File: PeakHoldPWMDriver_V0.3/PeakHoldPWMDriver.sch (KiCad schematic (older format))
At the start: 121 parts, among them J1 RND 205-00203, J2 RND 205-00205, Q1 2N7002, Q10 2N7002, Q11 2N7002, Q12 2N7002, Q13 TSM2309, Q14 IRLL 024N, Q15 TSM2309, Q16 IRLL 024N, Q17 TSM2309, Q18 TSM2309, Q19 TSM2309, Q2 2N7002, Q20 TSM2309, Q3 2N7002, Q4 2N7002, Q5 TSM2309, Q6 TSM2309, Q7 IRLL 024N, Q8 IRLL 024N, Q9 2N7002, U1 74LS32, U2 LM2901, U3 74LS74, U4 LTC6992, U5 74LS74, U6 LM340, U7 74LS08, U8 74LS08, U9 LM2904

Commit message: Some leftover updates
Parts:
- gave numbers to parts that had none: 1
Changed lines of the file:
@@
 	650  6550 700  6550
 $Comp
-L Amplifier_Operational:LM2904 U?
+L Amplifier_Operational:LM2904 U9
 U 2 1 5F7AED14
 P 1600 5700
-F 0 "U?" H 1600 6067 50  0000 C CNN
+F 0 "U9" H 1600 6067 50  0000 C CNN
 F 1 "LM2904" H 1600 5976 50  0000 C CNN
 F 2 "Package_SO:SO-8_3.9x4.9mm_P1.27mm" H 1600 5700 50  0001 C CNN

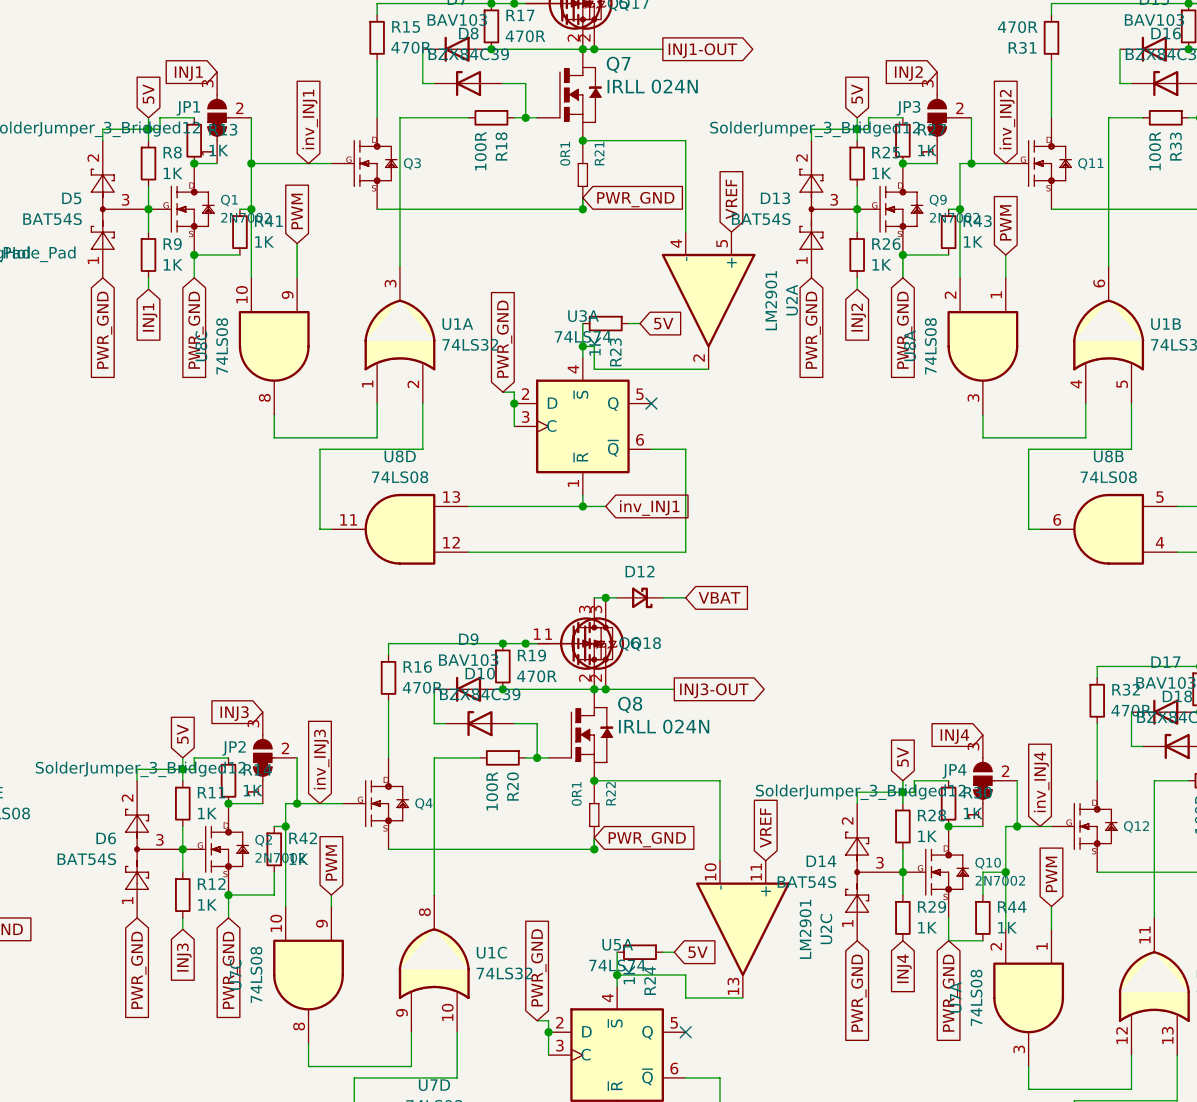
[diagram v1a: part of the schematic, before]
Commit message: updates values on 0.3 added 0.3.1
Updated resistor values for V0.3
Added V0.3.1 with new battery voltage compensation
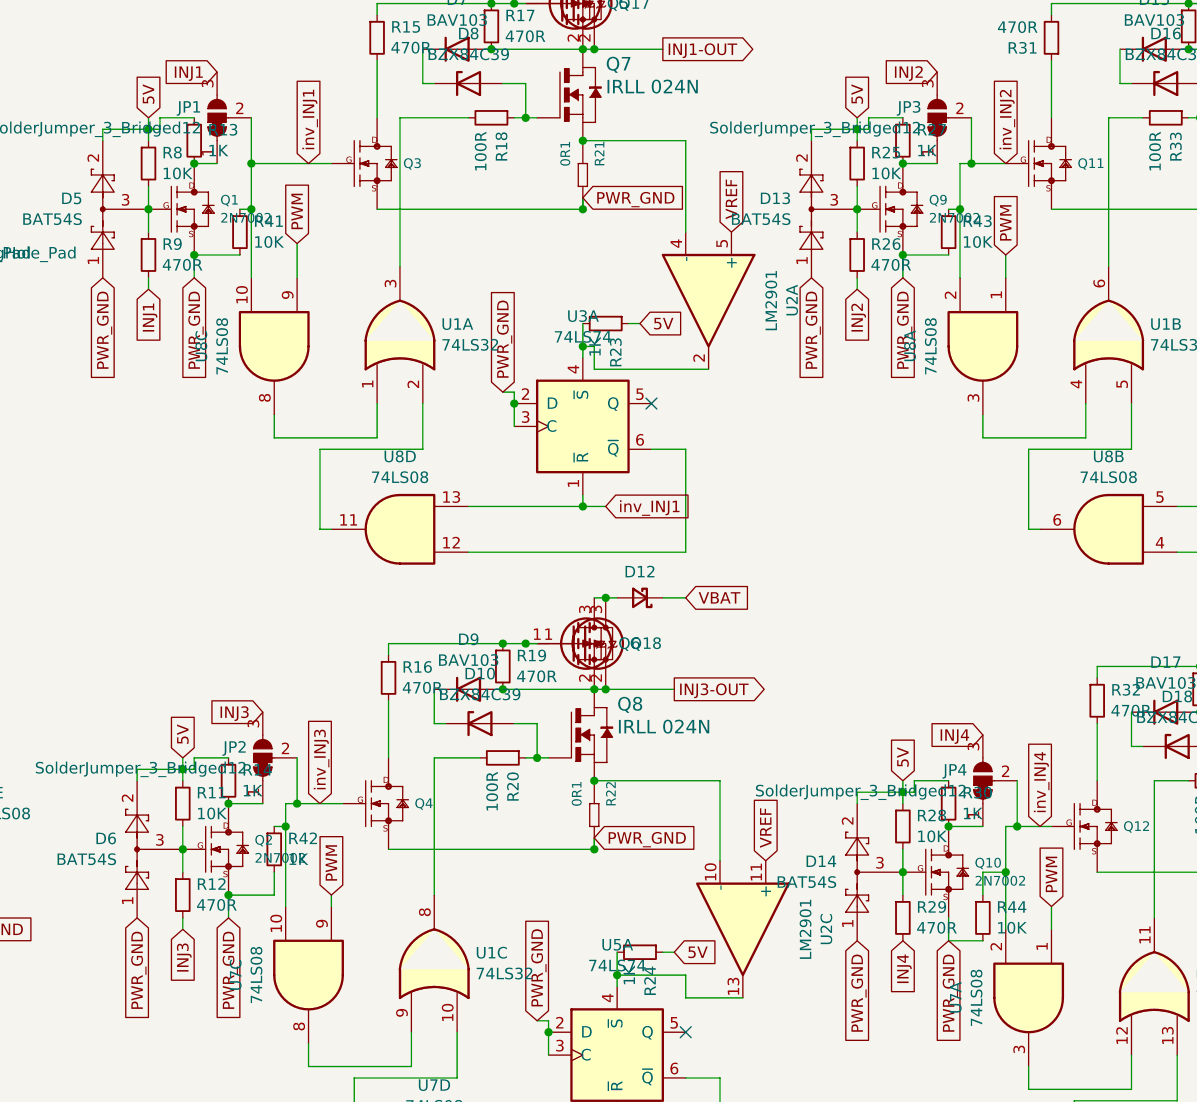
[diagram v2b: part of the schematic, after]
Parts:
- R11, R25, R28, R41, R43, R44, R8: value 1K -> 10K
- R12, R26, R29, R9: value 1K -> 470R
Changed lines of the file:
@@
 P 5200 1800
 F 0 "R8" H 5259 1846 50  0000 L CNN
-F 1 "1K" H 5259 1755 50  0000 L CNN
+F 1 "10K" H 5259 1755 50  0000 L CNN
 F 2 "Resistor_SMD:R_0603_1608Metric_Pad1.05x0.95mm_HandSolder" H 5200 1800 50  0001 C CNN
 F 3 "~" H 5200 1800 50  0001 C CNN
@@
 P 5200 2200
 F 0 "R9" H 5259 2246 50  0000 L CNN
-F 1 "1K" H 5259 2155 50  0000 L CNN
+F 1 "470R" H 5259 2155 50  0000 L CNN
 F 2 "Resistor_SMD:R_0603_1608Metric_Pad1.05x0.95mm_HandSolder" H 5200 2200 50  0001 C CNN
 F 3 "~" H 5200 2200 50  0001 C CNN
@@
 P 5350 4600
 F 0 "R11" H 5409 4646 50  0000 L CNN
-F 1 "1K" H 5409 4555 50  0000 L CNN
+F 1 "10K" H 5409 4555 50  0000 L CNN
 F 2 "Resistor_SMD:R_0603_1608Metric_Pad1.05x0.95mm_HandSolder" H 5350 4600 50  0001 C CNN
 F 3 "~" H 5350 4600 50  0001 C CNN
@@
 P 5350 5000
 F 0 "R12" H 5409 5046 50  0000 L CNN
-F 1 "1K" H 5409 4955 50  0000 L CNN
+F 1 "470R" H 5409 4955 50  0000 L CNN
 F 2 "Resistor_SMD:R_0603_1608Metric_Pad1.05x0.95mm_HandSolder" H 5350 5000 50  0001 C CNN
 F 3 "~" H 5350 5000 50  0001 C CNN
@@
 P 8500 4700
 F 0 "R28" H 8559 4746 50  0000 L CNN
-F 1 "1K" H 8559 4655 50  0000 L CNN
+F 1 "10K" H 8559 4655 50  0000 L CNN
 F 2 "Resistor_SMD:R_0603_1608Metric_Pad1.05x0.95mm_HandSolder" H 8500 4700 50  0001 C CNN
 F 3 "~" H 8500 4700 50  0001 C CNN
@@
 P 8500 5100
 F 0 "R29" H 8559 5146 50  0000 L CNN
-F 1 "1K" H 8559 5055 50  0000 L CNN
+F 1 "470R" H 8559 5055 50  0000 L CNN
 F 2 "Resistor_SMD:R_0603_1608Metric_Pad1.05x0.95mm_HandSolder" H 8500 5100 50  0001 C CNN
 F 3 "~" H 8500 5100 50  0001 C CNN
@@
 P 8300 1800
 F 0 "R25" H 8359 1846 50  0000 L CNN
-F 1 "1K" H 8359 1755 50  0000 L CNN
+F 1 "10K" H 8359 1755 50  0000 L CNN
 F 2 "Resistor_SMD:R_0603_1608Metric_Pad1.05x0.95mm_HandSolder" H 8300 1800 50  0001 C CNN
 F 3 "~" H 8300 1800 50  0001 C CNN
@@
 P 8300 2200
 F 0 "R26" H 8359 2246 50  0000 L CNN
-F 1 "1K" H 8359 2155 50  0000 L CNN
+F 1 "470R" H 8359 2155 50  0000 L CNN
 F 2 "Resistor_SMD:R_0603_1608Metric_Pad1.05x0.95mm_HandSolder" H 8300 2200 50  0001 C CNN
 F 3 "~" H 8300 2200 50  0001 C CNN
@@
 P 8850 5100
 F 0 "R44" H 8909 5146 50  0000 L CNN
-F 1 "1K" H 8909 5055 50  0000 L CNN
+F 1 "10K" H 8909 5055 50  0000 L CNN
 F 2 "Resistor_SMD:R_0603_1608Metric_Pad1.05x0.95mm_HandSolder" H 8850 5100 50  0001 C CNN
 F 3 "~" H 8850 5100 50  0001 C CNN
@@
 P 8700 2100
 F 0 "R43" H 8759 2146 50  0000 L CNN
-F 1 "1K" H 8759 2055 50  0000 L CNN
+F 1 "10K" H 8759 2055 50  0000 L CNN
 F 2 "Resistor_SMD:R_0603_1608Metric_Pad1.05x0.95mm_HandSolder" H 8700 2100 50  0001 C CNN
 F 3 "~" H 8700 2100 50  0001 C CNN
@@
 P 5600 2100
 F 0 "R41" H 5659 2146 50  0000 L CNN
-F 1 "1K" H 5659 2055 50  0000 L CNN
+F 1 "10K" H 5659 2055 50  0000 L CNN
 F 2 "Resistor_SMD:R_0603_1608Metric_Pad1.05x0.95mm_HandSolder" H 5600 2100 50  0001 C CNN
 F 3 "~" H 5600 2100 50  0001 C CNN
